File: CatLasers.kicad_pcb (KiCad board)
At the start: 2 copper layers, 42 parts, among them J1 Conn_01x02, J2 Programmer, J3 Conn_01x04, J4 Conn_01x04, J5 Conn_01x20, J6 IR Emitter, J7 Power Jumper, J8 IR Receiver, U1 MIC2288YD5-TR, U2 ESP32-WROOM-32E_(4MB_HIGH_TEM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

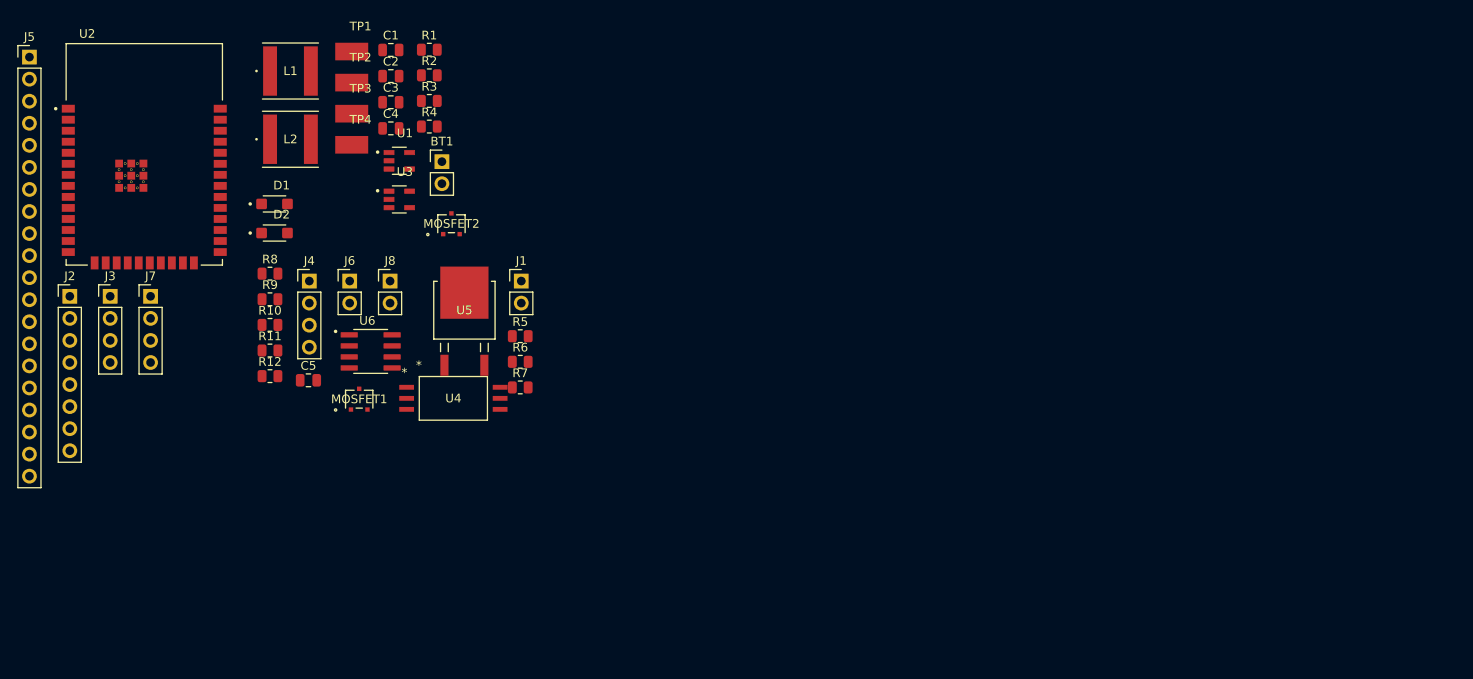
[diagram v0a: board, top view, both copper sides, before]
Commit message: Power Supply Layout
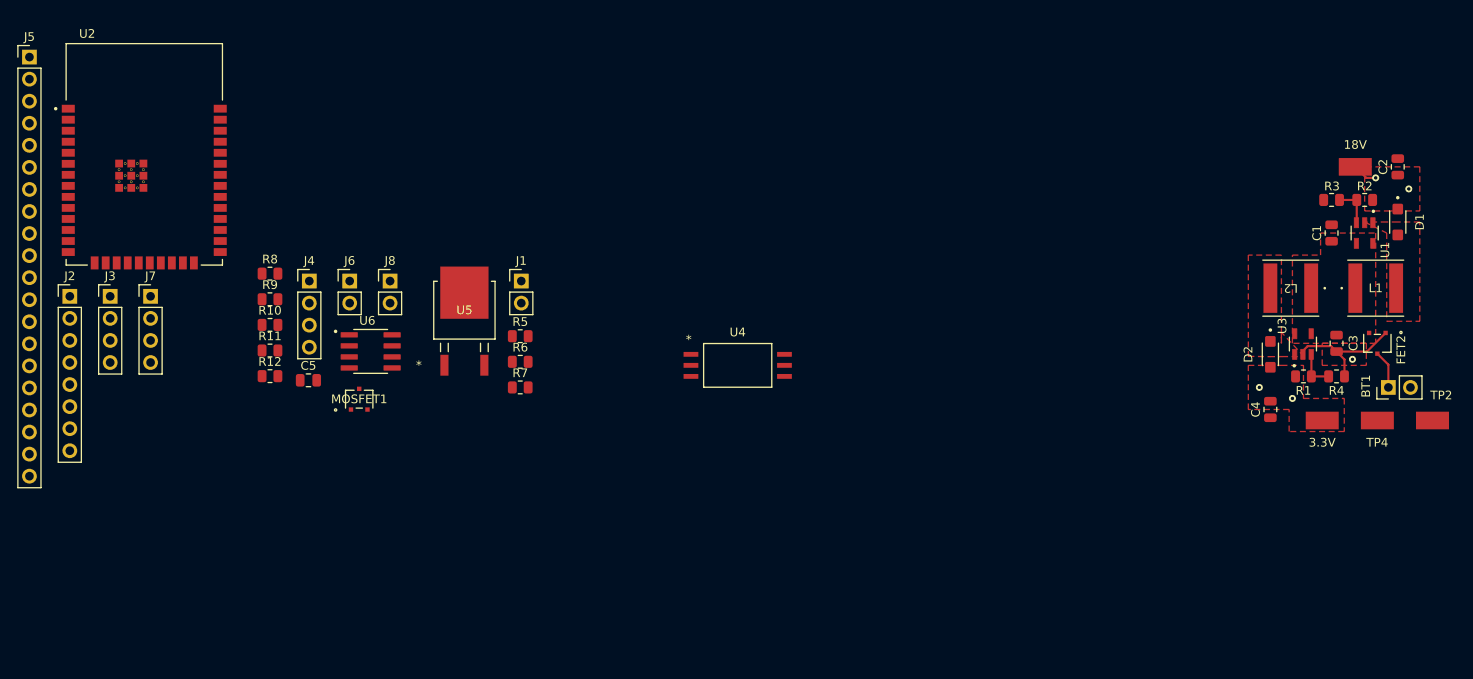
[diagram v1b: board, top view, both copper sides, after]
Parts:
- TP4: value Vin -> VBatt
- moved TP2 130.4 mm to (188.0, 62.2)
- moved D1 129.4 mm to (184.0, 39.4), turned to -90 degrees
- moved L1 127.5 mm to (181.4, 47.0)
- moved TP4 122.3 mm to (181.6, 62.2), turned to 180 degrees
- moved 3.3V 117.2 mm to (175.3, 62.2), turned to 180 degrees
- moved L2 116.5 mm to (171.6, 47.0), turned to 180 degrees
- moved C2 116.4 mm to (184.0, 33.0), turned to 90 degrees
- moved 18V 116.3 mm to (179.1, 33.0)
- moved D2 115.5 mm to (169.3, 54.6), turned to -90 degrees
- moved C3 112.4 mm to (176.9, 53.3), turned to 90 degrees
- moved BT1 112.1 mm to (182.9, 58.4), turned to 90 degrees
- moved U1 111.5 mm to (180.1, 40.6), turned to -90 degrees
- moved C1 110.4 mm to (176.3, 40.6), turned to 90 degrees
- moved R2 108.7 mm to (180.1, 36.8), turned to 180 degrees
- moved R4 108.4 mm to (176.9, 57.1), turned to 180 degrees
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- renumbered TP1 to 18V, TP3 to 3.3V, MOSFET2 to FET2
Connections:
- net Net-(BT1-+) renamed /PowerSupply/VBatt
- net Net-(D1-A) renamed /PowerSupply/SW_18
- net Net-(D2-A) renamed /PowerSupply/SW_3.3
- net Net-(U1-EN) renamed /PowerSupply/Vin
- net Net-(U1-FB) renamed /PowerSupply/FB_18
- net Net-(U3-FB) renamed /PowerSupply/FB_3.3
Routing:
- net GND: track 0.00 -> 14.5 mm, vias 0 -> 1
- net /PowerSupply/FB_18: track 0.00 -> 4.63 mm
- net /PowerSupply/FB_3.3: track 0.00 -> 4.53 mm
- net /PowerSupply/VBatt: track 0.00 -> 4.41 mm
- net 18V: track 0.00 -> 2.88 mm, vias 0 -> 2
- net 3.3V: vias 0 -> 2
- added copper zone on F.Cu, net /PowerSupply/SW_18
- added copper zone on F.Cu, net /PowerSupply/SW_3.3
- added copper zone on F.Cu, net /PowerSupply/Vin
- added copper zone on F.Cu, net 18V
- added copper zone on F.Cu, net 3.3V
- added copper zone on F.Cu, net GND

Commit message: Piezzo Layout
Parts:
- added J9: Conn_01x04, Connector_PinHeader_2.54mm:PinHeader_1x04_P2.54mm_Vertical, F.Cu at (91.4, 54.6)
- J1: value Conn_01x02 -> Piezzo
- moved J7 114.7 mm to (154.9, 43.2)
- moved U6 51.1 mm to (105.4, 86.4)
- moved J8 46.5 mm to (105.4, 73.7)
- moved J5 44.7 mm to (71.1, 21.6)
- moved J6 42.2 mm to (95.2, 73.7)
- moved J4 40.9 mm to (87.6, 74.9)
- moved R10 40.9 mm to (83.1, 80.0)
- moved R11 40.9 mm to (83.1, 82.9)
- moved C5 40.9 mm to (87.5, 86.4)
- moved MOSFET1 40.9 mm to (93.4, 88.5)
- moved R12 40.9 mm to (83.1, 85.9)
- moved R8 40.9 mm to (83.1, 74.1)
- moved R9 40.9 mm to (83.1, 77.0)
- moved R6 34.9 mm to (115.6, 43.2), turned to 90 degrees
- moved U5 34.7 mm to (109.2, 38.1), turned to 90 degrees
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- renumbered 18V to TP1, 3.3V to TP3
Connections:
- J5 pad 20: /IR Emitter + Receiver/Receiver -> unconnected-(J5-Pin_20-Pad20)
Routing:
- net /Buzzer/PWM: track 0.00 -> 11.1 mm
- net Net-(J1-Pin_1): track 0.00 -> 10.8 mm
- net Net-(U4-VOUT): track 0.00 -> 5.43 mm
- net Net-(U4-CATHODE): track 0.00 -> 4.08 mm
- net Net-(U5-Gate): track 0.00 -> 1.87 mm

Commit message: MCU Layout
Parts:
- moved FET2 123.6 mm to (58.0, 50.8)
- moved TP2 123.6 mm to (64.4, 59.7)
- moved TP4 123.6 mm to (58.0, 59.7)
- moved BT1 123.6 mm to (59.3, 55.9)
- moved C2 123.6 mm to (60.4, 30.5)
- moved C3 123.6 mm to (53.3, 50.8)
- moved C4 123.6 mm to (45.7, 58.4)
- moved D1 123.6 mm to (60.4, 36.8)
- moved D2 123.6 mm to (45.7, 52.1)
- moved L1 123.6 mm to (57.8, 44.5)
- moved L2 123.6 mm to (48.1, 44.5)
- moved R1 123.6 mm to (49.5, 54.6)
- moved R2 123.6 mm to (56.6, 34.3)
- moved R4 123.6 mm to (53.3, 54.6)
- moved TP1 123.6 mm to (55.5, 30.5)
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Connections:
- net /IR Emitter + Receiver/Receiver renamed /IR Emitter + Receiver/Rec_out
- net Net-(J4-Pin_1) renamed /IR Emitter + Receiver/Vsup
- net Net-(J4-Pin_3) renamed /IR Emitter + Receiver/Emit_Direct
- net Net-(J4-Pin_4) renamed /IR Emitter + Receiver/Emit_MOS
- net Net-(J8-Pin_2) renamed /IR Emitter + Receiver/Vrec
- net Net-(U6-1IN-) renamed /IR Emitter + Receiver/Vref
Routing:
- net Net-(J5-Pin_5): track 0.00 -> 64.0 mm, vias 0 -> 4
- net Net-(J5-Pin_6): track 0.00 -> 62.2 mm, vias 0 -> 2
- net Net-(J5-Pin_4): track 0.00 -> 60.9 mm, vias 0 -> 2
- net Net-(J5-Pin_17): track 0.00 -> 47.7 mm, vias 0 -> 4
- net Net-(J5-Pin_19): track 0.00 -> 45.7 mm, vias 0 -> 4
- net Net-(J5-Pin_1): track 0.00 -> 42.9 mm, vias 0 -> 4
- net Net-(J5-Pin_18): track 0.00 -> 42.6 mm, vias 0 -> 4
- net Net-(J5-Pin_16): track 0.00 -> 41.4 mm, vias 0 -> 2
- net Net-(J5-Pin_3): track 0.00 -> 41.1 mm, vias 0 -> 2
- net Net-(J5-Pin_2): track 0.00 -> 40.6 mm, vias 0 -> 2
- net Net-(J2-Pin_2): track 0.00 -> 39.9 mm, vias 0 -> 3
- net Net-(J2-Pin_3): track 0.00 -> 38.6 mm, vias 0 -> 3
- net Net-(J5-Pin_15): track 0.00 -> 38.3 mm, vias 0 -> 2
- net Net-(J2-Pin_5): track 0.00 -> 37.6 mm, vias 0 -> 3
- net Net-(J5-Pin_7): track 0.00 -> 28.8 mm, vias 0 -> 2
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
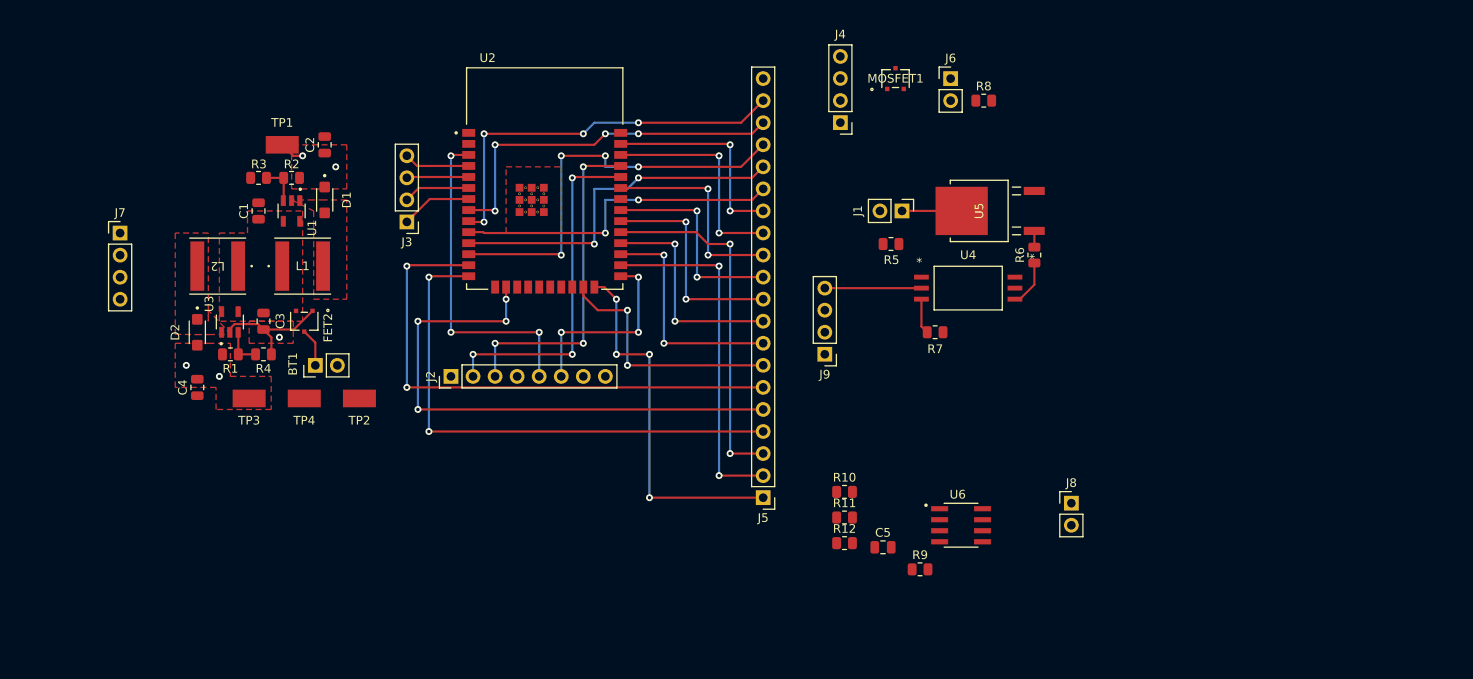
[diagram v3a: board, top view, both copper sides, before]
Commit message: Emitter, Receiver, and board outline
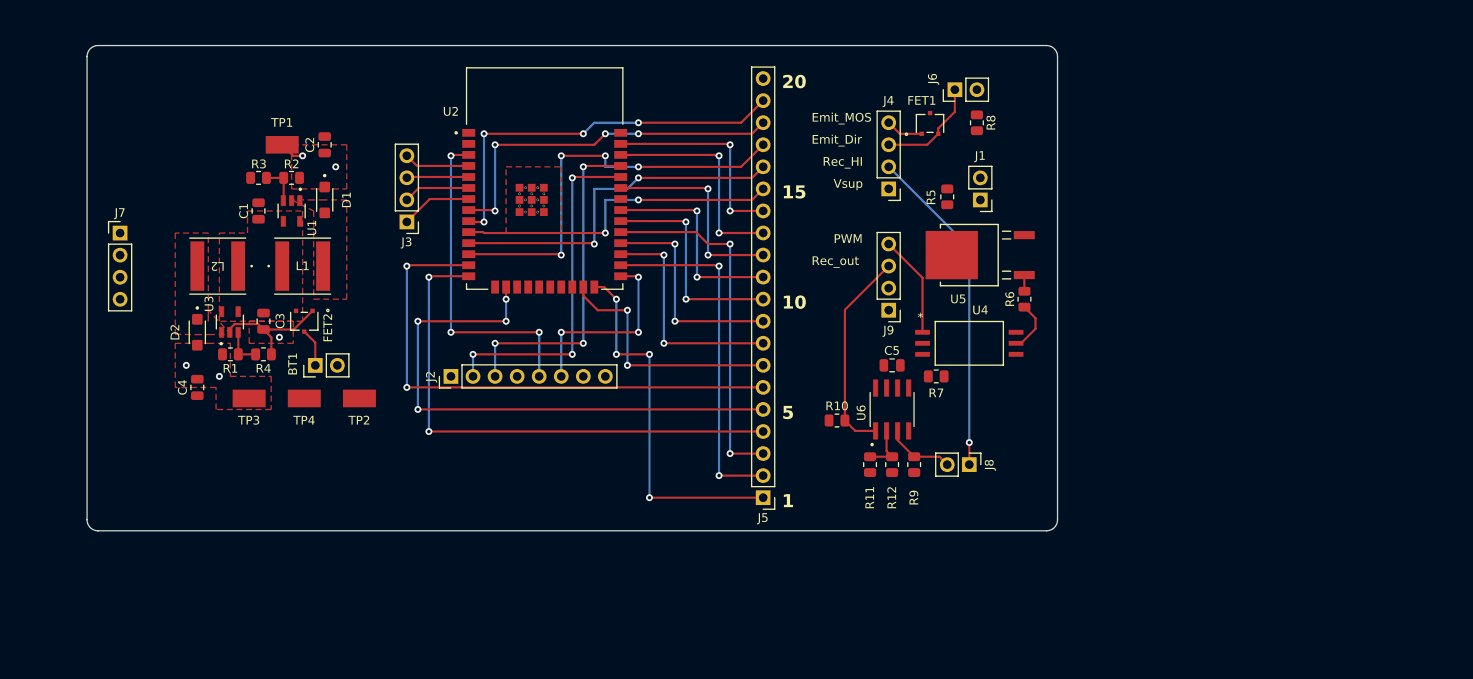
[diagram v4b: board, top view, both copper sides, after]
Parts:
- moved C5 21.0 mm to (125.7, 55.9)
- moved U6 15.5 mm to (125.7, 61.0), turned to 90 degrees
- moved J8 12.6 mm to (134.6, 67.3), turned to -90 degrees
- moved R9 12.1 mm to (128.3, 67.3), turned to -90 degrees
- moved R12 10.6 mm to (125.7, 67.3), turned to -90 degrees
- moved J4 9.44 mm to (125.3, 35.6)
- moved J1 9.11 mm to (135.9, 36.8), turned to 180 degrees
- moved J9 8.94 mm to (125.3, 49.5)
- moved R5 8.45 mm to (132.1, 36.5), turned to 90 degrees
- moved R10 8.27 mm to (119.4, 62.2)
- moved R11 6.76 mm to (123.2, 67.3), turned to 90 degrees
- moved FET1 6.52 mm to (130.1, 28.0)
- moved U4 6.36 mm to (134.6, 53.3)
- moved R6 5.21 mm to (141.0, 48.3)
- moved U5 5.21 mm to (134.6, 43.2)
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- renumbered MOSFET1 to FET1
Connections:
- net Net-(J4-Pin_2) renamed /IR Emitter + Receiver/RecSup
- J5 pad 20: unconnected-(J5-Pin_20-Pad20) -> GND
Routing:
- net /IR Emitter + Receiver/RecSup: track 0.00 -> 38.1 mm, vias 0 -> 1
- net /IR Emitter + Receiver/Rec_out: track 0.00 -> 23.9 mm
- net /IR Emitter + Receiver/Emit_Direct: track 0.00 -> 12.1 mm
- net /IR Emitter + Receiver/Vrec: track 0.00 -> 7.94 mm
- net Net-(J1-Pin_1): track 6.87 -> 0.00 mm
- net /IR Emitter + Receiver/Vref: track 0.00 -> 5.77 mm
- net /IR Emitter + Receiver/Emit_MOS: track 0.00 -> 4.34 mm
- net Net-(U4-CATHODE): track 4.08 -> 0.00 mm
- net /Buzzer/PWM: track 11.1 -> 11.8 mm
- net Net-(U4-VOUT): track 5.43 -> 5.95 mm
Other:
- board outline added: 111.8 x 55.9 mm
- board text added: "1"
- board text added: "10"
- board text added: "15"
- board text added: "20"
- board text added: "5"
- board text added: "Emit_Dir"
- board text added: "Emit_MOS"
- board text added: "PWM"
- board text added: "Rec_HI"
- board text added: "Rec_out"
- board text added: "Vsup"

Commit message: Routing Draft Finished
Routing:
- net 18V: track 2.88 -> 202.7 mm, vias 2 -> 9
- net GND: track 14.5 -> 68.3 mm, vias 1 -> 12
- net /IR Emitter + Receiver/Vsup: track 0.00 -> 40.8 mm, vias 0 -> 2
- net Net-(J1-Pin_1): track 0.00 -> 10.1 mm
- net /PowerSupply/VBatt: track 4.41 -> 8.75 mm
- net Net-(J6-Pin_2): track 0.00 -> 2.90 mm
- net Net-(U4-CATHODE): track 0.00 -> 2.81 mm
- added copper zone on B.Cu, net GND
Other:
- board size 111.8 x 55.9 mm -> 111.8 x 61 mm
